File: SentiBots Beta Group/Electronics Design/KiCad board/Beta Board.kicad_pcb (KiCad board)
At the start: 2 copper layers, 69.4 x 36.8 mm, 63 parts, among them P1 PWM out, P2 MCU GPIO, P3 USB OTG, P4 UART EDISON, P5 GND PWM, P7 BUZZER, P8 CONN_01X02, P9 BATT, Q1 MMBT3906, U1 TXB0108PWR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

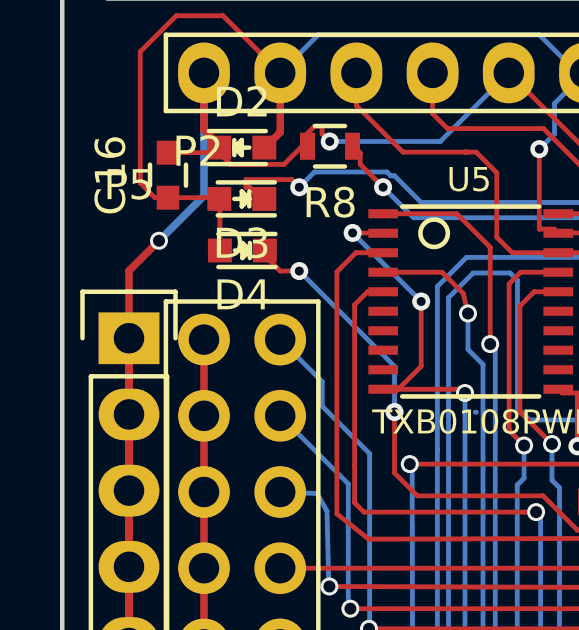
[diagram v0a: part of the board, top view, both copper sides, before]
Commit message: fixed silkscreen and added branding
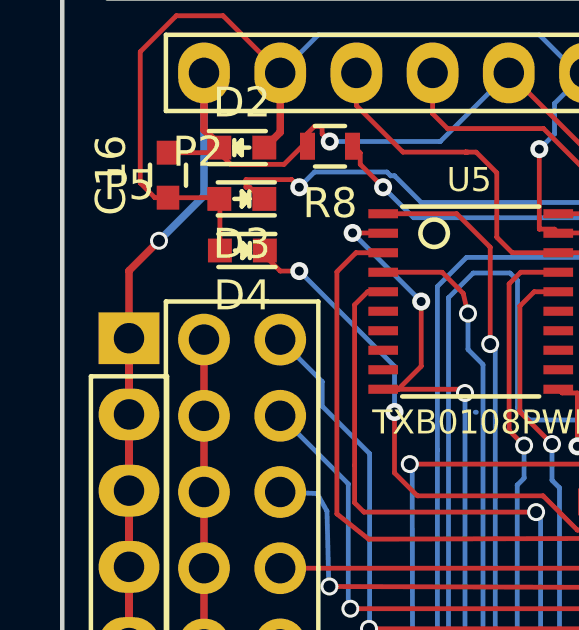
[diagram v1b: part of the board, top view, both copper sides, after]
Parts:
- P5: footprint Pin_Headers:Pin_Header_Straight_1x06 -> EdiCopter:Pin_Header_Straight_1x06
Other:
- board text added: "A MakerForce product"
- board text added: "Made by Sudharshan"
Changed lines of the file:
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@@
     (links 208)
     (no_connects 0)
-    (area 109.817381 79.035 190.45 118.785)
+    (area 111.149999 80.324999 180.715001 117.300001)
     (thickness 1.6)
-    (drawings 10)
+    (drawings 12)
     (tracks 1652)
     (zones 0)
@@
     )
   )
-  (module Pin_Headers:Pin_Header_Straight_1x06 (layer F.Cu)
+  (module EdiCopter:Pin_Header_Straight_1x06 (layer F.Cu)
     (at 113.45 91.775)
     (descr "Through hole pin header")
@@
     (fp_line (start 1.27 13.97) (end -1.27 13.97) (layer F.SilkS) (width 0.15))
     (fp_line (start -1.27 13.97) (end -1.27 1.27) (layer F.SilkS) (width 0.15))
-    (fp_line (start 1.55 -1.55) (end 1.55 0) (layer F.SilkS) (width 0.15))
     (fp_line (start 1.27 1.27) (end -1.27 1.27) (layer F.SilkS) (width 0.15))
-    (fp_line (start -1.55 0) (end -1.55 -1.55) (layer F.SilkS) (width 0.15))
-    (fp_line (start -1.55 -1.55) (end 1.55 -1.55) (layer F.SilkS) (width 0.15))
     (pad 1 thru_hole rect (at 0 0) (size 2.032 1.7272) (drill 1.016) (layers *.Cu *.Mask F.SilkS)
       (net 1 GND))
@@
     )
   )
+  (gr_text "A MakerForce product\n" (at 166.8 115.85) (layer B.SilkS)
+    (effects (font (size 1.5 1.5) (thickness 0.3)))
+  )
+  (gr_text "Made by Sudharshan" (at 123.525 115.775) (layer B.SilkS)
+    (effects (font (size 1.5 1.5) (thickness 0.3)))
+  )
   (gr_line (start 112.8 117.2) (end 112.8 117.225) (angle 90) (layer Edge.Cuts) (width 0.15))
